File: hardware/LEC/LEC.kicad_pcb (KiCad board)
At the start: 4 copper layers, 141.2 x 77.4 mm, 66 parts, among them J1 54-00278, J10 Conn_01x02, J11 54-00278, J12 54-00278, J13 54-00278, J14 54-00278, J2 54-00278, J3 54-00278, J4 54-00278, J5 54-00278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

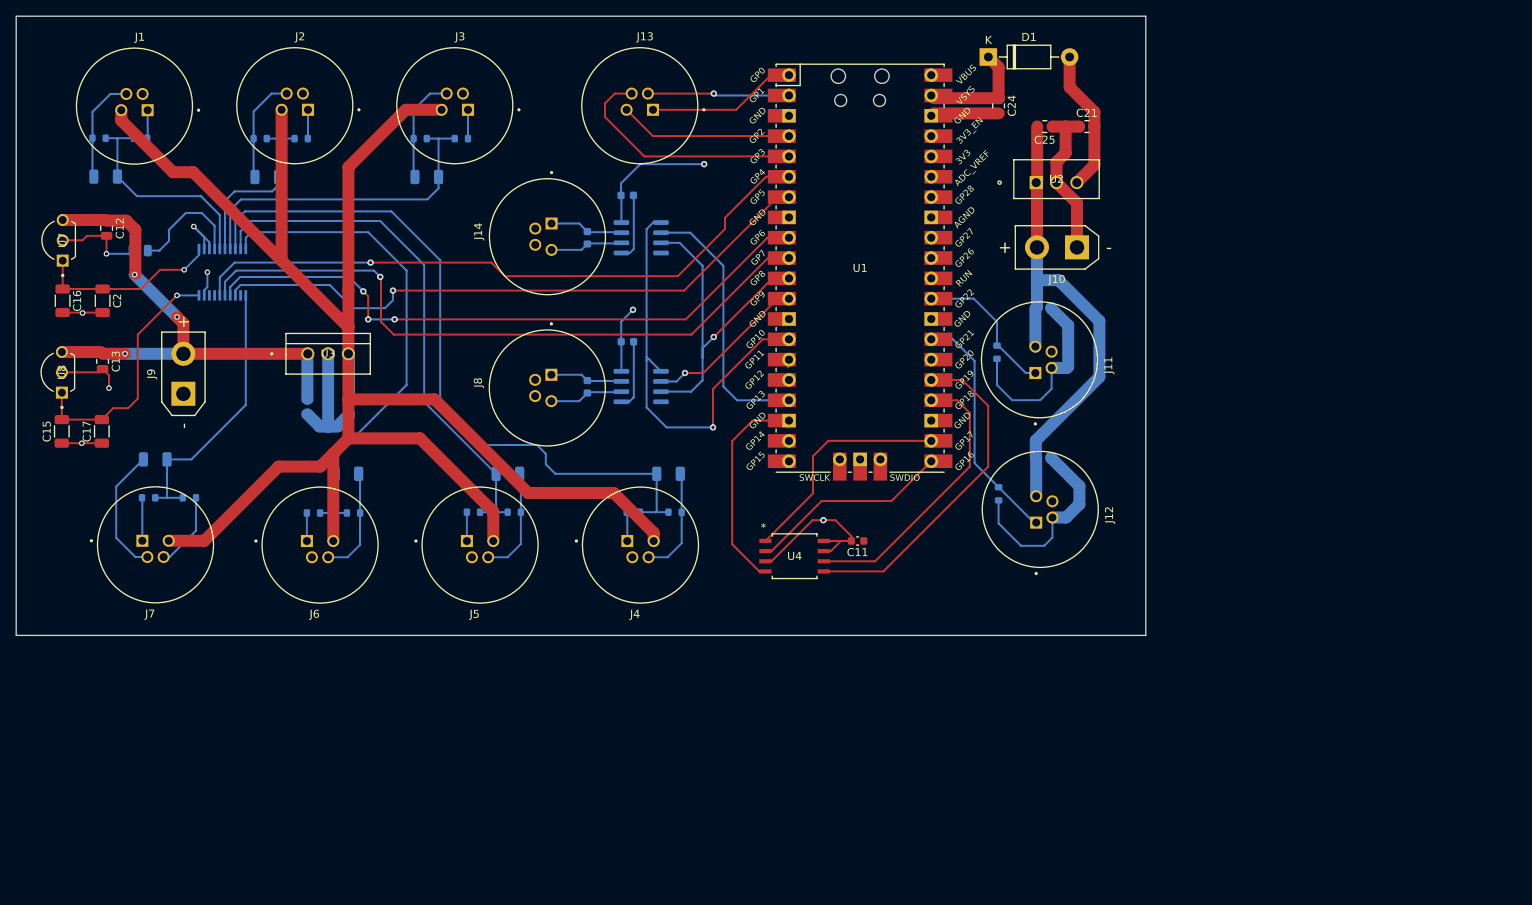
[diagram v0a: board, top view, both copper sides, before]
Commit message: Added mounting holes, ground planes, and via stiching
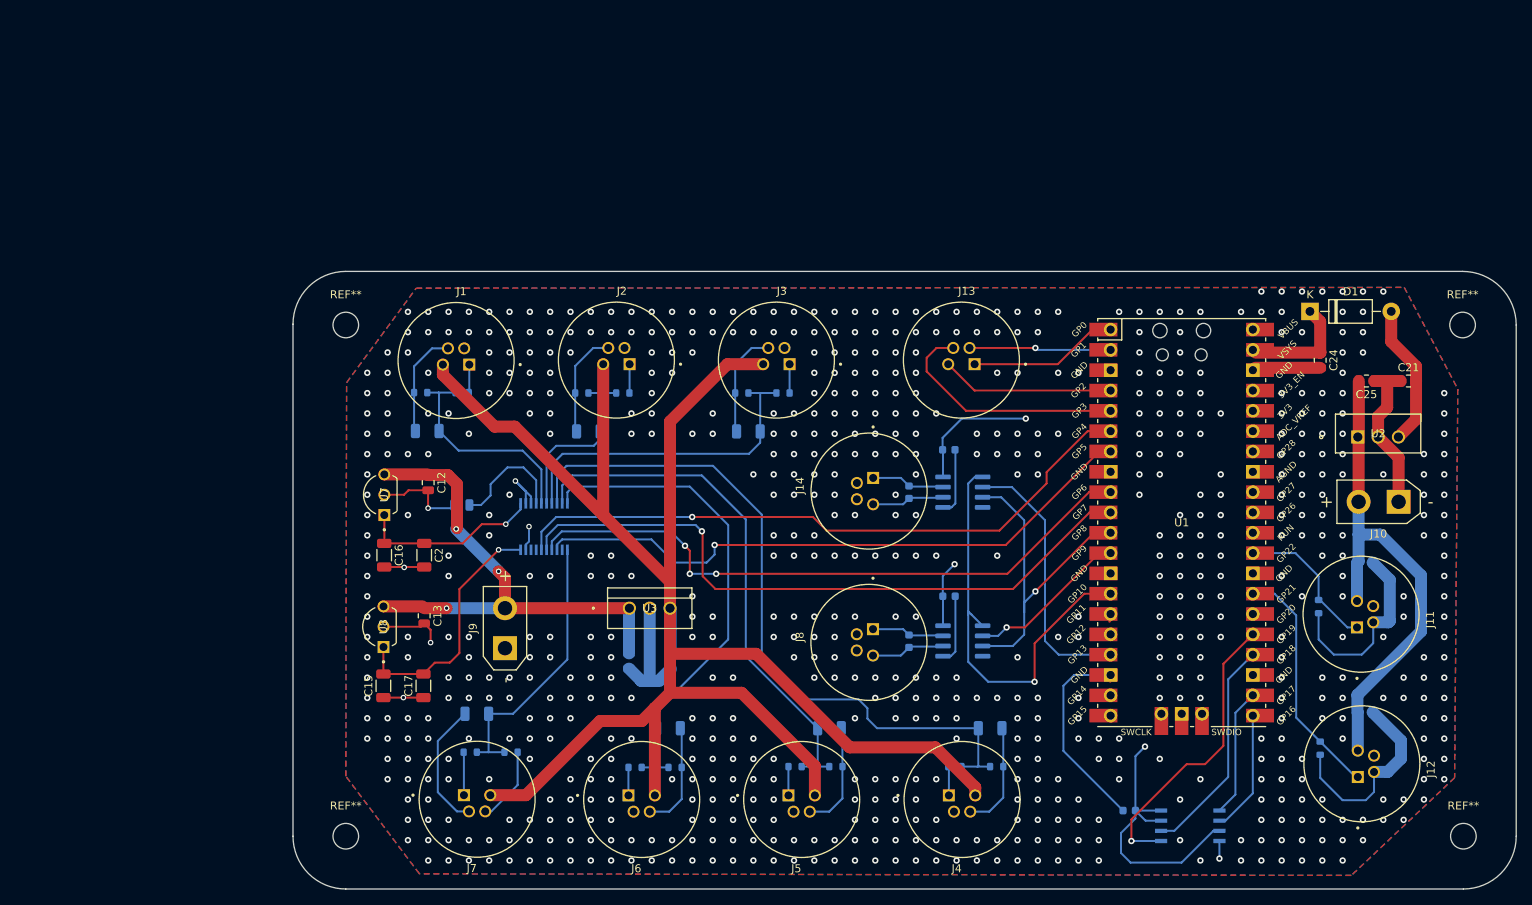
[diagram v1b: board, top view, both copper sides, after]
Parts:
- added REF**: MountingHole_3.2mm_M3_DIN965, MountingHole:MountingHole_3.2mm_M3_DIN965, F.Cu at (205.6, 56.5)
- added REF**: MountingHole_3.2mm_M3_DIN965, MountingHole:MountingHole_3.2mm_M3_DIN965, F.Cu at (205.7, 120.4)
- added REF**: MountingHole_3.2mm_M3_DIN965, MountingHole:MountingHole_3.2mm_M3_DIN965, F.Cu at (66.0, 120.4)
- added REF**: MountingHole_3.2mm_M3_DIN965, MountingHole:MountingHole_3.2mm_M3_DIN965, F.Cu at (66.0, 56.5)
- C11, U4: moved to B.Cu
- moved U4 59.8 mm to (171.6, 119.1), turned to 180 degrees
- moved C22 51.3 mm to (193.4, 104.9)
- moved R16 51.3 mm to (187.8, 109.4)
- moved C18 51.3 mm to (193.4, 86.2)
- moved C21 51.3 mm to (198.8, 63.5)
- moved C24 51.3 mm to (187.8, 60.9)
- moved C25 51.3 mm to (193.6, 63.5)
- moved D1 51.3 mm to (186.5, 54.8)
- moved R13 51.3 mm to (81.6, 109.9)
- moved R8 51.3 mm to (147.4, 111.7)
- moved U1 51.3 mm to (170.5, 81.2)
- moved C1 51.3 mm to (76.2, 69.8)
- moved C10 51.3 mm to (141.4, 90.4)
- moved C23 51.3 mm to (136.4, 96.0)
- moved C26 51.3 mm to (136.4, 77.4)
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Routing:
- net /GPIO17 (CS): track 31.1 -> 18.6 mm
- net +3.3V: track 166.4 -> 178.4 mm
- net /GPIO16 (MISO): track 25.9 -> 15.8 mm
- net /GPIO18 (SCK): track 37.5 -> 29.9 mm
- net /GPIO19 (MOSI): track 42.0 -> 37.2 mm, vias 0 -> 1
- net GND: track 283.3 -> 284.1 mm, vias 6 -> 711
- added copper zone on B.Cu, net GND
- added copper zone on F.Cu, net GND
- added copper zone on In1.Cu, net GND
- added copper zone on In2.Cu, net GND
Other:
- board size 141.2 x 77.4 mm -> 152.9 x 77.2 mm

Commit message: Added labeling, moved ADC decoupling caps closer to ADC
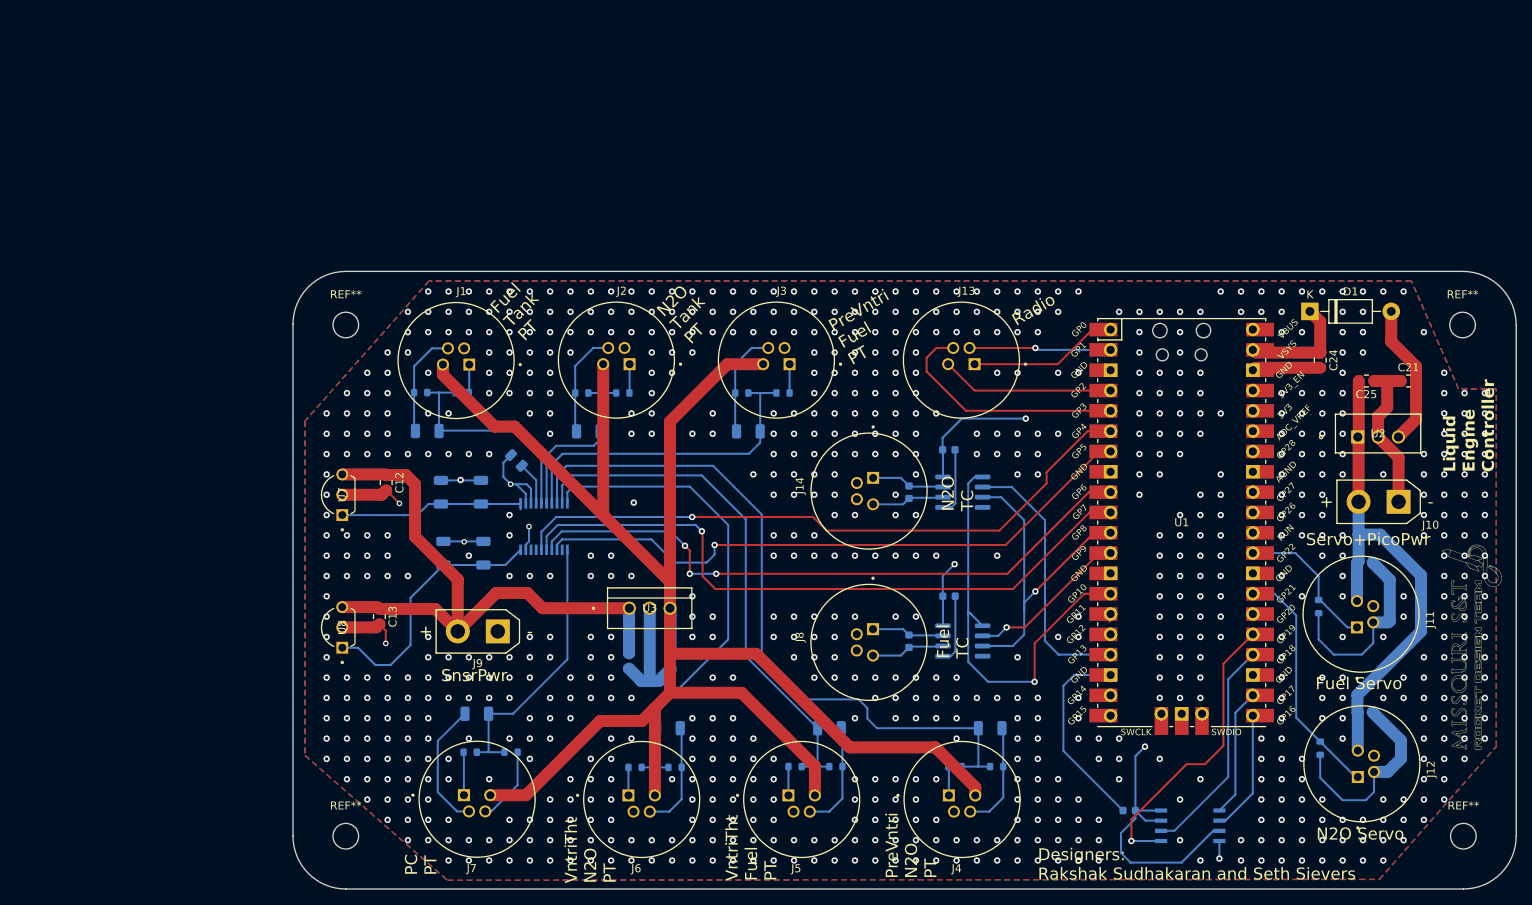
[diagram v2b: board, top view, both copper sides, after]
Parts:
- added G***: LOGO, RDTLogo:RDT_Logo, F.Cu at (206.8, 96.8)
- C15, C16, C17, C2: moved to B.Cu
- moved C15 20.8 mm to (83.2, 85.0), turned to -90 degrees
- moved C17 16.8 mm to (78.2, 85.0), turned to -90 degrees
- moved C16 14.4 mm to (82.9, 77.4), turned to 90 degrees
- moved C14 8.81 mm to (87.3, 73.4), turned to -45 degrees
- moved C2 8.15 mm to (77.9, 77.4), turned to 90 degrees
- moved C13 5.60 mm to (70.2, 93.0)
- moved C12 5.25 mm to (71.0, 76.2)
- moved U7 5.25 mm to (65.6, 80.3)
- moved U8 5.15 mm to (65.6, 96.8)
- moved J9 2.28 mm to (85.0, 94.8), turned to 180 degrees
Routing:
- net /ADC_Power_Circuit/VIN: track 64.2 -> 75.7 mm, vias 3 -> 0
- net Net-(U15-REFIN+/OUT): track 14.7 -> 5.44 mm
- net GND: track 284.1 -> 286.4 mm, vias 711 -> 832
- net /lowPassFilter/Sig_{out}: track 27.6 -> 29.0 mm
- net /ADC_Power_Circuit/DVDDOUT: track 31.6 -> 32.6 mm, vias 1 -> 0
- net /ADC_Power_Circuit/AVDDOUT: track 23.1 -> 23.6 mm, vias 1 -> 0
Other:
- board text added: "Designers: Rakshak Sudhakaran and Seth Sievers"
- board text added: "Flash IC"
- board text added: "Fuel Servo"
- board text added: "Fuel TC"
- board text added: "Fuel Tank PT"
- board text added: "Liquid Engine Controller"
- board text added: "N2O Servo"
- board text added: "N2O TC"
- board text added: "N2O Tank PT"
- board text added: "PC PT"
- board text added: "PreVntri Fuel PT"
- board text added: "PreVntri N2O PT"
- board text added: "Radio"
- board text added: "Servo+PicoPwr"
- board text added: "SnsrPwr"
- board text added: "VntriTht Fuel PT"
- board text added: "VntriTht N2O PT"

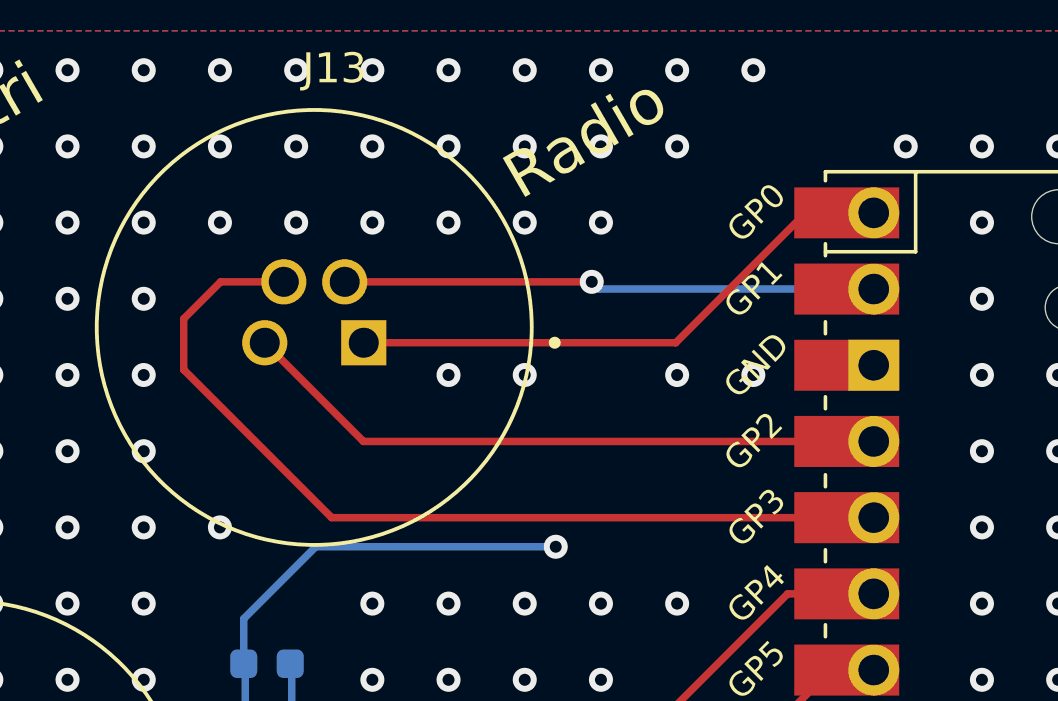
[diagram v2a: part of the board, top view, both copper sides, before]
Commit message: Updated pin mapping of radio connector for cleaner routing
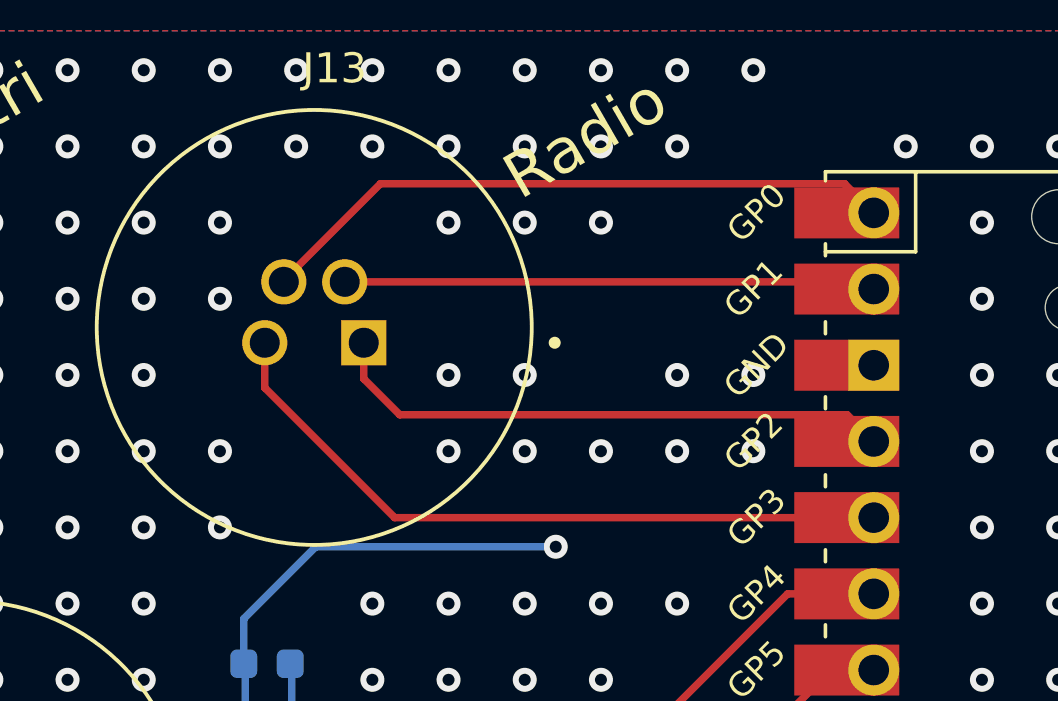
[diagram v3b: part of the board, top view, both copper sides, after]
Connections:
- J13 pad 1: /GPIO0 (MISO) -> /GPIO2 (SCK)
- J13 pad 3: /GPIO2 (SCK) -> /GPIO3 (MOSI)
- J13 pad 4: /GPIO3 (MOSI) -> /GPIO0 (MISO)
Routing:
- net /GPIO3 (MOSI): track 30.6 -> 23.6 mm
- net /GPIO0 (MISO): track 18.8 -> 23.7 mm
- net /GPIO2 (SCK): track 21.7 -> 19.1 mm
- net /GPIO1 (CS): vias 1 -> 0
- net GND: vias 832 -> 837

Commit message: Final updates
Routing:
- net GND: track 286.4 -> 19.7 mm, vias 837 -> 239
- net /ADC_Power_Circuit/DVDDOUT: track 32.6 -> 29.9 mm
- net +3.3V: track 178.4 -> 180.5 mm
- net /GPIO13 (CS): track 33.5 -> 32.2 mm
